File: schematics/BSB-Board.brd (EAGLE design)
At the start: 29.7 x 53.3 mm, 23 parts, among them Q1 BC 547A, Q11 BC 557A, Q12 BC 547A, U1 4N25, U2 4N25

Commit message: Bugfixes
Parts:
- removed SJ4_RPI: Close for RPi, jumper:SJ
- added SJ2_RPI: Close for RPi, jumper:SJ
- moved ARD_8-15 17.8 mm to (1.78, 2.54), flipped to the bottom
- moved SJ3_RPI 7.62 mm to (2.54, 47.0)
- renumbered ARD_SUP to ARD_5V
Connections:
- net N$11 renamed ARD_PI_TXD
- net A14-RXD-ARD: now also ARD_8-15.7; no longer ARD_8-15.2
- net A15-TXD-ARD: now also ARD_8-15.8; no longer ARD_8-15.1
- net GND-ARD: now also SJ2_RPI.2; no longer SJ3_RPI.2
- net GPIO18-3V3-PI: now also SJ3_RPI.1; no longer SJ4_RPI.1
- net PIN6-GND-PI: now also SJ2_RPI.1; no longer SJ3_RPI.1
- net VCC: now also SJ3_RPI.2; no longer SJ4_RPI.2
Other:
- board text added: "B"
- board text added: "C"
- board text added: "E"
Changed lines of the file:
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@@
 <text x="13.843" y="32.385" size="1.016" layer="27" rot="R90">DB
 CL+</text>
+<text x="13.335" y="41.021" size="1.016" layer="21" font="vector" ratio="15">C</text>
+<text x="15.875" y="41.021" size="1.016" layer="21" font="vector" ratio="15">B</text>
+<text x="18.542" y="41.021" size="1.016" layer="21" font="vector" ratio="15">E</text>
+<text x="16.129" y="22.987" size="1.016" layer="21" font="vector" ratio="15">C</text>
+<text x="18.669" y="22.987" size="1.016" layer="21" font="vector" ratio="15">B</text>
+<text x="21.336" y="22.987" size="1.016" layer="21" font="vector" ratio="15">E</text>
+<text x="13.335" y="47.371" size="1.016" layer="21" font="vector" ratio="15">C</text>
+<text x="15.875" y="47.371" size="1.016" layer="21" font="vector" ratio="15">B</text>
+<text x="18.542" y="47.371" size="1.016" layer="21" font="vector" ratio="15">E</text>
 </plain>
 <attributes>
@@
 <elements>
 <element name="ARD_GND" library="SparkFun-Connectors" package="1X02" value="" x="22.098" y="7.62"/>
-<element name="ARD_SUP" library="SparkFun-Connectors" package="1X02" value="" x="22.098" y="50.8"/>
+<element name="ARD_5V" library="SparkFun-Connectors" package="1X02" value="" x="22.098" y="50.8"/>
 <element name="U1" library="optocoupler" package="DIL06" value="4N25" x="6.223" y="12.446" rot="R270">
 <attribute name="MF" value="" x="6.223" y="12.446" size="1.778" layer="27" rot="R270" display="off"/>
@@
 <attribute name="VALUE" x="12.446" y="36.068" size="1.27" layer="27" ratio="10"/>
 </element>
-<element name="SJ4_RPI" library="jumper" package="SJ" value="Close for RPi" x="2.54" y="46.99" rot="R270"/>
-<element name="SJ3_RPI" library="jumper" package="SJ" value="Close for RPi" x="10.16" y="46.99" rot="R270"/>
+<element name="SJ3_RPI" library="jumper" package="SJ" value="Close for RPi" x="2.54" y="46.99" rot="R270"/>
+<element name="SJ2_RPI" library="jumper" package="SJ" value="Close for RPi" x="10.16" y="46.99" rot="R270"/>
 <element name="SJ1_ARD" library="jumper" package="SJ" value="Close for Arduino" x="21.971" y="46.99" rot="R90"/>
 <element name="RPI_2-12" library="SparkFun-Connectors" package="1X06" value="" x="1.778" y="50.927">
@@
 </element>
 <element name="ARD_23-53" library="SparkFun-Connectors" package="1X16" value="" x="24.638" y="10.16" rot="R90"/>
-<element name="ARD_8-15" library="SparkFun-Connectors" package="1X08_ROUND" value="" x="19.558" y="2.54" rot="R180"/>
+<element name="ARD_8-15" library="SparkFun-Connectors" package="1X08_ROUND" value="" x="1.778" y="2.54" rot="MR180"/>
 </elements>
 <signals>
 <signal name="A14-RXD-ARD">
-<contactref element="R11" pad="1"/>
-<contactref element="R12" pad="2"/>
 <contactref element="U1" pad="5"/>
-<wire x1="2.4384" y1="30.1752" x2="2.4384" y2="29.2608" width="0.3048" layer="16"/>
-<wire x1="1.2192" y1="31.3944" x2="2.4384" y2="30.1752" width="0.3048" layer="16"/>
-<wire x1="1.2192" y1="34.7472" x2="1.2192" y2="31.3944" width="0.3048" layer="16"/>
-<wire x1="9.4488" y1="42.9768" x2="1.2192" y2="34.7472" width="0.3048" layer="16"/>
-<wire x1="10.0584" y1="42.9768" x2="9.4488" y2="42.9768" width="0.3048" layer="16"/>
-<wire x1="2.4384" y1="29.2608" x2="2.54" y2="29.21" width="0.3048" layer="16"/>
-<wire x1="10.0584" y1="42.9768" x2="10.16" y2="43.18" width="0.3048" layer="16"/>
 <wire x1="9.7536" y1="13.4112" x2="9.7536" y2="12.4968" width="0.3048" layer="1"/>
 <wire x1="6.7056" y1="16.4592" x2="9.7536" y2="13.4112" width="0.3048" layer="1"/>
@@
 <wire x1="2.4384" y1="28.956" x2="1.2192" y2="27.7368" width="0.3048" layer="1"/>
 <wire x1="9.7536" y1="12.4968" x2="10.033" y2="12.446" width="0.3048" layer="1"/>
-<wire x1="2.4384" y1="28.956" x2="2.54" y2="29.21" width="0.3048" layer="1"/>
-<contactref element="ARD_8-15" pad="2"/>
+<contactref element="R11" pad="1"/>
+<contactref element="R12" pad="2"/>
+<contactref element="ARD_8-15" pad="7"/>
+<wire x1="2.4384" y1="30.1752" x2="2.4384" y2="29.2608" width="0.3048" layer="16"/>
+<wire x1="1.2192" y1="31.3944" x2="2.4384" y2="30.1752" width="0.3048" layer="16"/>
+<wire x1="1.2192" y1="34.7472" x2="1.2192" y2="31.3944" width="0.3048" layer="16"/>
+<wire x1="9.4488" y1="42.9768" x2="1.2192" y2="34.7472" width="0.3048" layer="16"/>
+<wire x1="10.0584" y1="42.9768" x2="9.4488" y2="42.9768" width="0.3048" layer="16"/>
+<wire x1="2.4384" y1="29.2608" x2="2.54" y2="29.21" width="0.3048" layer="16"/>
+<wire x1="10.0584" y1="42.9768" x2="10.16" y2="43.18" width="0.3048" layer="16"/>
 <wire x1="16.764" y1="5.7912" x2="16.764" y2="2.7432" width="0.3048" layer="16"/>
 <wire x1="12.8016" y1="9.7536" x2="16.764" y2="5.7912" width="0.3048" layer="16"/>
@@
 <wire x1="16.764" y1="2.7432" x2="17.018" y2="2.54" width="0.3048" layer="16"/>
 <wire x1="10.0584" y1="12.192" x2="10.033" y2="12.446" width="0.3048" layer="16"/>
+<wire x1="2.4384" y1="28.956" x2="2.54" y2="29.21" width="0.3048" layer="1"/>
 </signal>
 <signal name="A15-TXD-ARD">
@@
 <wire x1="10.3632" y1="34.4424" x2="10.16" y2="34.29" width="0.3048" layer="16"/>
 <wire x1="13.716" y1="39.3192" x2="13.716" y2="39.37" width="0.3048" layer="16"/>
-<contactref element="ARD_8-15" pad="1"/>
+<contactref element="ARD_8-15" pad="8"/>
 <wire x1="19.812" y1="8.8392" x2="19.812" y2="2.7432" width="0.3048" layer="16"/>
 <wire x1="21.6408" y1="10.668" x2="19.812" y2="8.8392" width="0.3048" layer="16"/>
@@
 <wire x1="21.336" y1="21.336" x2="21.463" y2="21.336" width="0.3048" layer="1"/>
 </signal>
-<signal name="N$11">
+<signal name="ARD_PI_TXD">
 <contactref element="U2" pad="1"/>
 <contactref element="R3" pad="1"/>
@@
 <contactref element="Q11" pad="E"/>
 <contactref element="R11" pad="2"/>
-<contactref element="SJ4_RPI" pad="2"/>
+<contactref element="SJ3_RPI" pad="2"/>
 <contactref element="SJ1_ARD" pad="1"/>
 <wire x1="2.4384" y1="44.8056" x2="2.4384" y2="46.0248" width="0.3048" layer="1"/>
@@
 <contactref element="U1" pad="4"/>
 <contactref element="Q12" pad="E"/>
-<contactref element="SJ3_RPI" pad="2"/>
+<contactref element="SJ2_RPI" pad="2"/>
 <wire x1="2.7432" y1="20.1168" x2="2.7432" y2="21.0312" width="0.3048" layer="1"/>
 <wire x1="6.096" y1="16.764" x2="2.7432" y2="20.1168" width="0.3048" layer="1"/>
@@
 </signal>
 <signal name="GPIO18-3V3-PI">
-<contactref element="SJ4_RPI" pad="1"/>
+<contactref element="SJ3_RPI" pad="1"/>
 <contactref element="RPI_2-12" pad="6"/>
 <wire x1="3.3528" y1="47.5488" x2="2.7432" y2="47.5488" width="0.3048" layer="1"/>
@@
 </signal>
 <signal name="PIN6-GND-PI">
-<contactref element="SJ3_RPI" pad="1"/>
+<contactref element="SJ2_RPI" pad="1"/>
 <contactref element="RPI_2-12" pad="3"/>
 <wire x1="7.0104" y1="50.9016" x2="10.16" y2="47.752" width="0.3048" layer="1"/>
@@
 </signal>
 <signal name="5V-ARD">
-<contactref element="ARD_SUP" pad="2"/>
+<contactref element="ARD_5V" pad="2"/>
 <contactref element="SJ1_ARD" pad="2"/>
 <wire x1="22.2504" y1="48.4632" x2="22.2504" y2="47.8536" width="0.3048" layer="1"/>

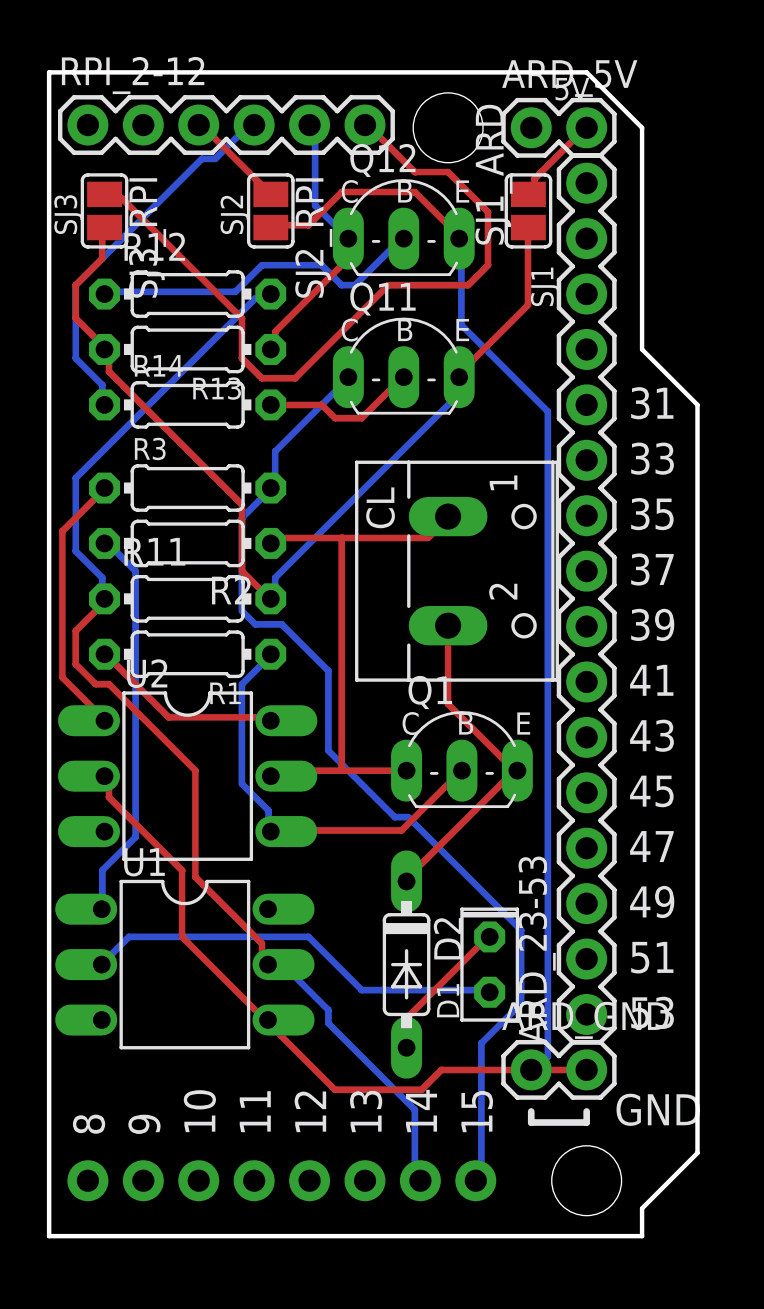
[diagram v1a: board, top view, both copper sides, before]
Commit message: Clarified layout
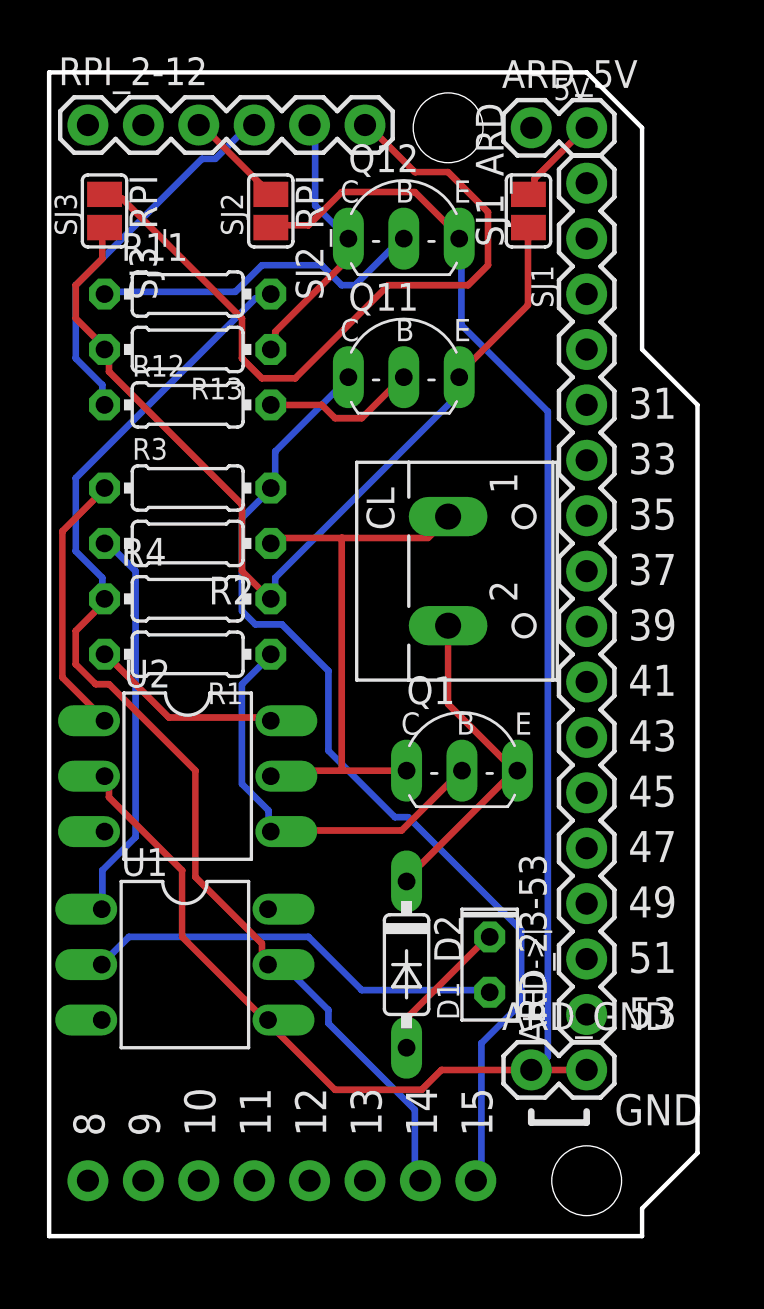
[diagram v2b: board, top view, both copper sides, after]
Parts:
- removed R14: 10k, resistor:0204/7
- added R4: 4k7, resistor:0204/7
- D1: value LED->| -> (none)
- R11: value 4k7 -> 47k
- R12: value 47k -> 10k
- moved R11 14.0 mm to (6.35, 43.2)
- moved R12 5.08 mm to (6.35, 38.1)
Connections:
- net A14-RXD-ARD: now also R11.2, R4.1; no longer R11.1, R12.2
- net GPIO14-TXD-PI: now also R12.1; no longer R14.1
- net N$6: now also R11.1; no longer R12.1
- net N$9: now also R12.2; no longer R14.2
- net VCC: now also R4.2; no longer R11.2
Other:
- board text added: "LED->|"
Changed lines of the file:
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@@
 <text x="15.875" y="47.371" size="1.016" layer="21" font="vector" ratio="15">B</text>
 <text x="18.542" y="47.371" size="1.016" layer="21" font="vector" ratio="15">E</text>
+<text x="22.733" y="9.779" size="1.016" layer="21" font="vector" ratio="15" rot="R90">LED-&gt;|</text>
 </plain>
 <attributes>
@@
 <attribute name="VALUE" x="5.3594" y="33.6804" size="1.27" layer="27" ratio="10"/>
 </element>
-<element name="D1" library="led" package="LED2X5" value="LED-&gt;|" x="20.193" y="12.446" rot="R90"/>
+<element name="D1" library="led" package="LED2X5" value="" x="20.193" y="12.446" rot="R90"/>
 <element name="CL" library="con-wago-500" package="W237-102" value="" x="19.558" y="30.48" smashed="yes" rot="R270">
 <attribute name="MF" value="" x="19.558" y="30.48" size="1.778" layer="27" rot="R270" display="off"/>
@@
 <attribute name="VALUE" x="12.446" y="42.418" size="1.27" layer="27" ratio="10"/>
 </element>
-<element name="R12" library="resistor" package="0204/7" value="47k" x="6.35" y="43.18" smashed="yes">
+<element name="R11" library="resistor" package="0204/7" value="47k" x="6.35" y="43.18" smashed="yes">
 <attribute name="NAME" x="3.302" y="44.704" size="1.27" layer="25" ratio="10"/>
 <attribute name="SPICEPREFIX" value="R" x="6.35" y="43.18" size="1.778" layer="27" display="off"/>
 <attribute name="VALUE" x="5.4864" y="42.545" size="1.27" layer="27" ratio="10"/>
 </element>
-<element name="R11" library="resistor" package="0204/7" value="4k7" x="6.35" y="29.21" smashed="yes">
+<element name="R4" library="resistor" package="0204/7" value="4k7" x="6.35" y="29.21" smashed="yes">
 <attribute name="NAME" x="3.302" y="30.734" size="1.27" layer="25" ratio="10"/>
 <attribute name="SPICEPREFIX" value="R" x="6.35" y="29.21" size="1.778" layer="27" display="off"/>
 <attribute name="VALUE" x="5.4864" y="28.702" size="1.27" layer="27" ratio="10"/>
 </element>
-<element name="R14" library="resistor" package="0204/7" value="10k" x="6.35" y="38.1" smashed="yes">
+<element name="R12" library="resistor" package="0204/7" value="10k" x="6.35" y="38.1" smashed="yes">
 <attribute name="NAME" x="3.81" y="39.3954" size="0.9906" layer="25" ratio="10"/>
 <attribute name="SPICEPREFIX" value="R" x="6.35" y="38.1" size="1.778" layer="27" display="off"/>
@@
 <wire x1="2.4384" y1="28.956" x2="1.2192" y2="27.7368" width="0.3048" layer="1"/>
 <wire x1="9.7536" y1="12.4968" x2="10.033" y2="12.446" width="0.3048" layer="1"/>
-<contactref element="R11" pad="1"/>
-<contactref element="R12" pad="2"/>
+<contactref element="R4" pad="1"/>
+<contactref element="R11" pad="2"/>
 <contactref element="ARD_8-15" pad="7"/>
 <wire x1="2.4384" y1="30.1752" x2="2.4384" y2="29.2608" width="0.3048" layer="16"/>
@@
 <contactref element="R13" pad="2"/>
 <contactref element="Q11" pad="E"/>
-<contactref element="R11" pad="2"/>
+<contactref element="R4" pad="2"/>
 <contactref element="SJ3_RPI" pad="2"/>
 <contactref element="SJ1_ARD" pad="1"/>
@@
 <signal name="N$9">
 <contactref element="Q11" pad="B"/>
-<contactref element="R14" pad="2"/>
+<contactref element="R12" pad="2"/>
 <wire x1="12.4968" y1="38.1" x2="10.16" y2="38.1" width="0.3048" layer="1"/>
 <wire x1="13.1064" y1="37.4904" x2="12.4968" y2="38.1" width="0.3048" layer="1"/>
@@
 </signal>
 <signal name="GPIO14-TXD-PI">
-<contactref element="R14" pad="1"/>
+<contactref element="R12" pad="1"/>
 <contactref element="RPI_2-12" pad="4"/>
 <wire x1="2.4384" y1="39.0144" x2="2.4384" y2="38.1" width="0.3048" layer="16"/>
@@
 <signal name="N$6">
 <contactref element="Q12" pad="B"/>
-<contactref element="R12" pad="1"/>
+<contactref element="R11" pad="1"/>
 <wire x1="8.5344" y1="43.2816" x2="2.7432" y2="43.2816" width="0.3048" layer="16"/>
 <wire x1="9.7536" y1="44.5008" x2="8.5344" y2="43.2816" width="0.3048" layer="16"/>
